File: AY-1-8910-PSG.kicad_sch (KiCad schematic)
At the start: 2 parts

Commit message: first draft
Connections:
- net GND: now reaches U?.1 (GND)
- net GND: now also A?.29 (GND), A?.4 (GND)
- net at U?.22 (CLOCK): now also A?.12 (D9)
- net A2: now reaches U?.27 (BDIR)
- net A2: now also A?.21 (A2)
- net A1: now reaches U?.28 (BC2)
- net A1: now also A?.20 (A1)
- net A0: now reaches U?.29 (BC1)
- net A0: now also A?.19 (A0)
- net A3: now reaches U?.30 (DA7)
- net A3: now also A?.22 (A3)
- net at U?.31 (DA6): now also A?.11 (D8)
- net at U?.32 (DA5): now also A?.10 (D7)
- net at U?.33 (DA4): now also A?.9 (D6)
- net at U?.34 (DA3): now also A?.8 (D5)
- net at U?.35 (DA2): now also A?.7 (D4)
- net at U?.36 (DA1): now also A?.6 (D3)
- net at U?.37 (DA0): now also A?.5 (D2)
- net +5V: now reaches U?.40 (VCC)
- net +5V: now also A?.27 (+5V)
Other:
- moved on the sheet: A?
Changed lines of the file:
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@@
 (kicad_sch (version 20211123) (generator eeschema)
   (paper "A4")
+  (wire (pts (xy 139.7 80.01) (xy 167.64 80.01))
+    (stroke (width 0) (type default) (color 0 0 0 0))
+  )
+  (wire (pts (xy 139.7 82.55) (xy 167.64 82.55))
+    (stroke (width 0) (type default) (color 0 0 0 0))
+  )
+  (wire (pts (xy 139.7 115.57) (xy 154.94 115.57))
+    (stroke (width 0) (type default) (color 0 0 0 0))
+  )
+  (wire (pts (xy 87.63 69.85) (xy 99.06 69.85))
+    (stroke (width 0) (type default) (color 0 0 0 0))
+  )
+  (wire (pts (xy 139.7 92.71) (xy 167.64 92.71))
+    (stroke (width 0) (type default) (color 0 0 0 0))
+  )
+  (wire (pts (xy 154.94 95.25) (xy 154.94 115.57))
+    (stroke (width 0) (type default) (color 0 0 0 0))
+  )
+  (wire (pts (xy 139.7 77.47) (xy 167.64 77.47))
+    (stroke (width 0) (type default) (color 0 0 0 0))
+  )
+  (wire (pts (xy 167.64 95.25) (xy 154.94 95.25))
+    (stroke (width 0) (type default) (color 0 0 0 0))
+  )
+  (wire (pts (xy 139.7 90.17) (xy 167.64 90.17))
+    (stroke (width 0) (type default) (color 0 0 0 0))
+  )
+  (wire (pts (xy 139.7 87.63) (xy 167.64 87.63))
+    (stroke (width 0) (type default) (color 0 0 0 0))
+  )
+  (wire (pts (xy 139.7 85.09) (xy 167.64 85.09))
+    (stroke (width 0) (type default) (color 0 0 0 0))
+  )
+  (global_label "A3" (shape input) (at 139.7 95.25 0) (fields_autoplaced)
+    (effects (font (size 1.27 1.27)) (justify left))
+    (property "Intersheet References" "${INTERSHEET_REFS}" (id 0) (at 144.4112 95.1706 0)
+      (effects (font (size 1.27 1.27)) (justify left) hide)
+    )
+  )
+  (global_label "A0" (shape input) (at 139.7 97.79 0) (fields_autoplaced)
+    (effects (font (size 1.27 1.27)) (justify left))
+    (property "Intersheet References" "${INTERSHEET_REFS}" (id 0) (at 144.4112 97.7106 0)
+      (effects (font (size 1.27 1.27)) (justify left) hide)
+    )
+  )
+  (global_label "A1" (shape input) (at 139.7 100.33 0) (fields_autoplaced)
+    (effects (font (size 1.27 1.27)) (justify left))
+    (property "Intersheet References" "${INTERSHEET_REFS}" (id 0) (at 144.4112 100.2506 0)
+      (effects (font (size 1.27 1.27)) (justify left) hide)
+    )
+  )
+  (global_label "A2" (shape input) (at 193.04 95.25 0) (fields_autoplaced)
+    (effects (font (size 1.27 1.27)) (justify left))
+    (property "Intersheet References" "${INTERSHEET_REFS}" (id 0) (at 197.7512 95.1706 0)
+      (effects (font (size 1.27 1.27)) (justify left) hide)
+    )
+  )
+  (global_label "A1" (shape input) (at 193.04 92.71 0) (fields_autoplaced)
+    (effects (font (size 1.27 1.27)) (justify left))
+    (property "Intersheet References" "${INTERSHEET_REFS}" (id 0) (at 197.7512 92.6306 0)
+      (effects (font (size 1.27 1.27)) (justify left) hide)
+    )
+  )
+  (global_label "A2" (shape input) (at 139.7 102.87 0) (fields_autoplaced)
+    (effects (font (size 1.27 1.27)) (justify left))
+    (property "Intersheet References" "${INTERSHEET_REFS}" (id 0) (at 144.4112 102.7906 0)
+      (effects (font (size 1.27 1.27)) (justify left) hide)
+    )
+  )
+  (global_label "A0" (shape input) (at 193.04 90.17 0) (fields_autoplaced)
+    (effects (font (size 1.27 1.27)) (justify left))
+    (property "Intersheet References" "${INTERSHEET_REFS}" (id 0) (at 197.7512 90.0906 0)
+      (effects (font (size 1.27 1.27)) (justify left) hide)
+    )
+  )
+  (global_label "A3" (shape input) (at 193.04 97.79 0) (fields_autoplaced)
+    (effects (font (size 1.27 1.27)) (justify left))
+    (property "Intersheet References" "${INTERSHEET_REFS}" (id 0) (at 197.7512 97.7106 0)
+      (effects (font (size 1.27 1.27)) (justify left) hide)
+    )
+  )
   (symbol (lib_id "xenir_v6:AY-3-8910") (at 119.38 62.23 0) (unit 1)
     (in_bom yes) (on_board yes) (fields_autoplaced)
@@
     (pin "9")
   )
-  (symbol (lib_id "MCU_Module:Arduino_Nano_Every") (at 180.34 92.71 0) (unit 1)
-    (in_bom yes) (on_board yes) (fields_autoplaced)
-    (property "Reference" "A?" (id 0) (at 182.3594 118.11 0)
+  (symbol (lib_id "power:GND") (at 87.63 69.85 0) (unit 1)
+    (in_bom yes) (on_board yes) (fields_autoplaced)
+    (property "Reference" "#PWR?" (id 0) (at 87.63 76.2 0)
+      (effects (font (size 1.27 1.27)) hide)
+    )
+    (property "Value" "GND" (id 1) (at 87.63 74.93 0))
+    (property "Footprint" "" (id 2) (at 87.63 69.85 0)
+      (effects (font (size 1.27 1.27)) hide)
+    )
+    (property "Datasheet" "" (id 3) (at 87.63 69.85 0)
+      (effects (font (size 1.27 1.27)) hide)
+    )
+    (pin "1")
+  )
+  (symbol (lib_id "power:GND") (at 180.34 115.57 0) (unit 1)
+    (in_bom yes) (on_board yes) (fields_autoplaced)
+    (property "Reference" "#PWR?" (id 0) (at 180.34 121.92 0)
+      (effects (font (size 1.27 1.27)) hide)
+    )
+    (property "Value" "GND" (id 1) (at 180.34 120.65 0))
+    (property "Footprint" "" (id 2) (at 180.34 115.57 0)
+      (effects (font (size 1.27 1.27)) hide)
+    )
+    (property "Datasheet" "" (id 3) (at 180.34 115.57 0)
+      (effects (font (size 1.27 1.27)) hide)
+    )
+    (pin "1")
+  )
+  (symbol (lib_id "power:+5V") (at 139.7 69.85 0) (unit 1)
+    (in_bom yes) (on_board yes) (fields_autoplaced)
+    (property "Reference" "#PWR?" (id 0) (at 139.7 73.66 0)
+      (effects (font (size 1.27 1.27)) hide)
+    )
+    (property "Value" "+5V" (id 1) (at 139.7 64.77 0))
+    (property "Footprint" "" (id 2) (at 139.7 69.85 0)
+      (effects (font (size 1.27 1.27)) hide)
+    )
+    (property "Datasheet" "" (id 3) (at 139.7 69.85 0)
+      (effects (font (size 1.27 1.27)) hide)
+    )
+    (pin "1")
+  )
+  (symbol (lib_id "power:+5V") (at 185.42 64.77 0) (unit 1)
+    (in_bom yes) (on_board yes) (fields_autoplaced)
+    (property "Reference" "#PWR?" (id 0) (at 185.42 68.58 0)
+      (effects (font (size 1.27 1.27)) hide)
+    )
+    (property "Value" "+5V" (id 1) (at 185.42 59.69 0))
+    (property "Footprint" "" (id 2) (at 185.42 64.77 0)
+      (effects (font (size 1.27 1.27)) hide)
+    )
+    (property "Datasheet" "" (id 3) (at 185.42 64.77 0)
+      (effects (font (size 1.27 1.27)) hide)
+    )
+    (pin "1")
+  )
+  (symbol (lib_id "MCU_Module:Arduino_Nano_Every") (at 180.34 90.17 0) (unit 1)
+    (in_bom yes) (on_board yes) (fields_autoplaced)
+    (property "Reference" "A?" (id 0) (at 182.3594 115.57 0)
       (effects (font (size 1.27 1.27)) (justify left))
     )
-    (property "Value" "Arduino_Nano_Every" (id 1) (at 182.3594 120.65 0)
+    (property "Value" "Arduino_Nano_Every" (id 1) (at 182.3594 118.11 0)
       (effects (font (size 1.27 1.27)) (justify left))
     )
-    (property "Footprint" "Module:Arduino_Nano" (id 2) (at 180.34 92.71 0)
+    (property "Footprint" "Module:Arduino_Nano" (id 2) (at 180.34 90.17 0)
       (effects (font (size 1.27 1.27) italic) hide)
     )
-    (property "Datasheet" "https://content.arduino.cc/assets/NANOEveryV3.0_sch.pdf" (id 3) (at 180.34 92.71 0)
+    (property "Datasheet" "https://content.arduino.cc/assets/NANOEveryV3.0_sch.pdf" (id 3) (at 180.34 90.17 0)
       (effects (font (size 1.27 1.27)) hide)
     )
@@
   )
   (symbol_instances
+    (path "/318a80bc-bb47-479b-9ad6-cc89ccf1f537"
+      (reference "#PWR?") (unit 1) (value "GND") (footprint "")
+    )
+    (path "/79c82aa0-68c2-4c99-9665-4d614e59696c"
+      (reference "#PWR?") (unit 1) (value "GND") (footprint "")
+    )
+    (path "/a2348e69-57ed-4427-8ba5-b20356f146a3"
+      (reference "#PWR?") (unit 1) (value "+5V") (footprint "")
+    )
+    (path "/d8b2571c-5c58-4db9-bc3d-b5cf98bfa251"
+      (reference "#PWR?") (unit 1) (value "+5V") (footprint "")
+    )
     (path "/e9678172-8957-4dd3-80d7-8fc9e74cf769"
       (reference "A?") (unit 1) (value "Arduino_Nano_Every") (footprint "Module:Arduino_Nano")

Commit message: update
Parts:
- added C1: 220uF, symbol Device:C_Polarized
- added C2: 47nF, symbol xenir:Capacitor
- added C3: 220nF, symbol xenir:Capacitor
- added C?: 10uF, symbol Device:C_Polarized
- added R1: 10, symbol xenir:Resistor
- added R2: 510, symbol xenir:Resistor
- added R3: 5.1k, symbol xenir:Resistor
- added R4: 1k, symbol xenir:Resistor
- added U1: LM386, symbol Amplifier_Audio:LM386
- gave numbers to parts that had none: 2
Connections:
- net GND: now also C3.1, C?.2, R1.1, R2.1, R4.1, U1.2 (-), U1.4 (GND)
- net at U2.3 (CHAN_B): now also U2.38 (CHAN_C), U2.4 (CHAN_A), R3.1, R4.2
- new net: C3.2, R2.2, R3.2, U1.3 (+)
- new net: C2.1, R1.2
- new net: C1.1, C2.2, U1.5
- new net +10V: C?.1, U1.6 (V+)
- new net AUDIO_OUT: C1.2
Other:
- moved on the sheet: A1, U2

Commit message: gg
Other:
- note added: "Bus Control"
- note added: "Data Lines"
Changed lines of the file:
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@@
     (stroke (width 0) (type default) (color 0 0 0 0))
+  )
+  (text "Bus\nControl" (at 195.58 109.22 90)
+    (effects (font (size 1.27 1.27)) (justify left bottom))
+  )
+  (text "Data Lines" (at 203.2 96.52 90)
+    (effects (font (size 1.27 1.27)) (justify left bottom))
   )
   (global_label "A3" (shape input) (at 186.69 100.33 0) (fields_autoplaced)

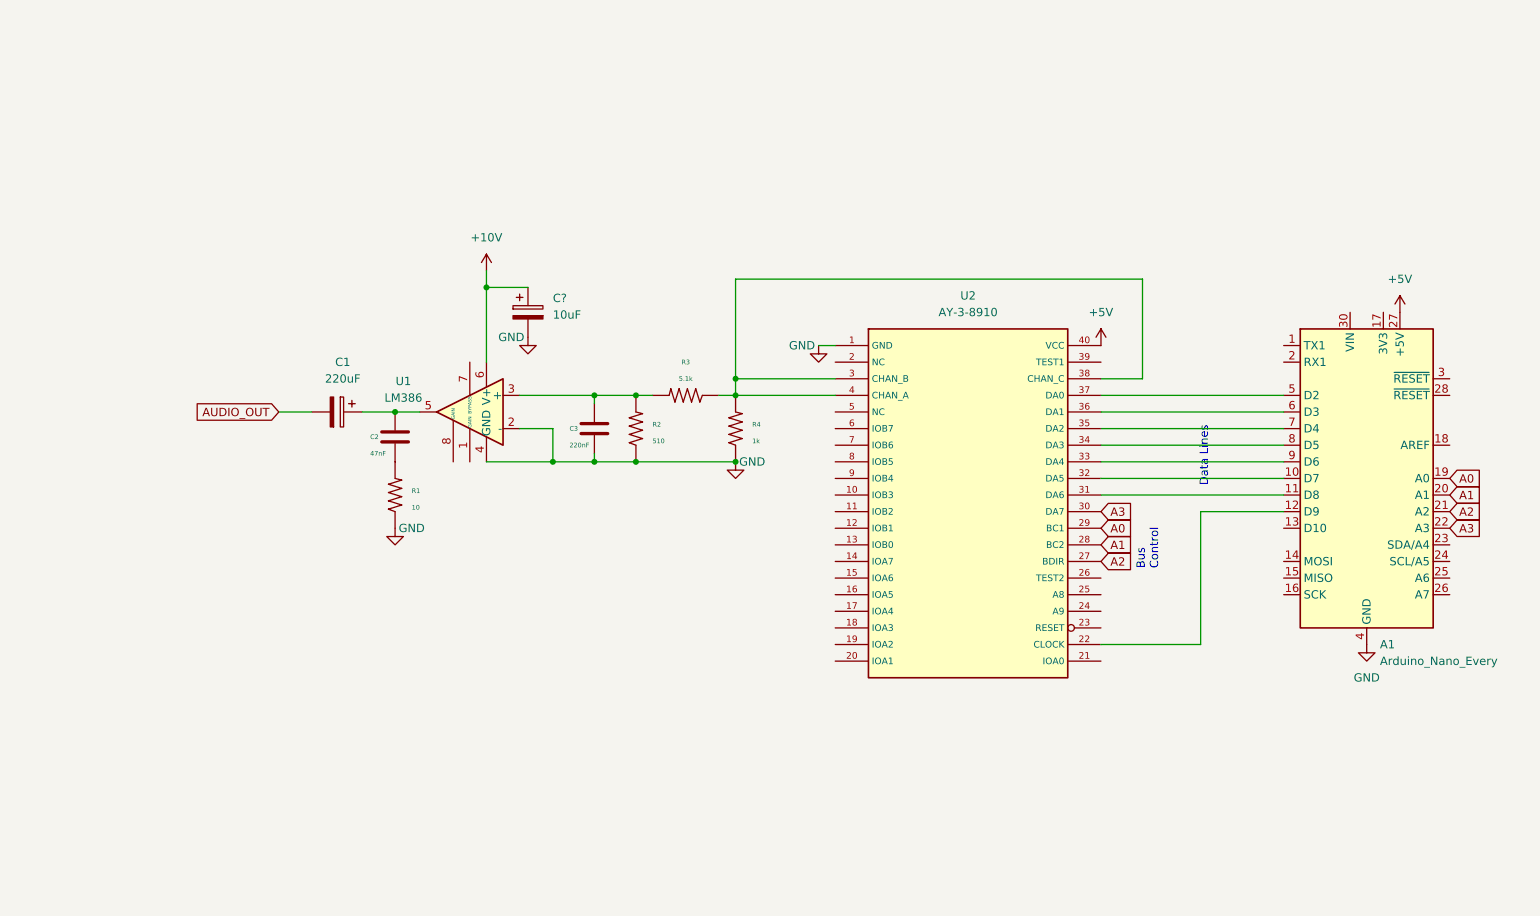
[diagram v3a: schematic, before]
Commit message: added esp32
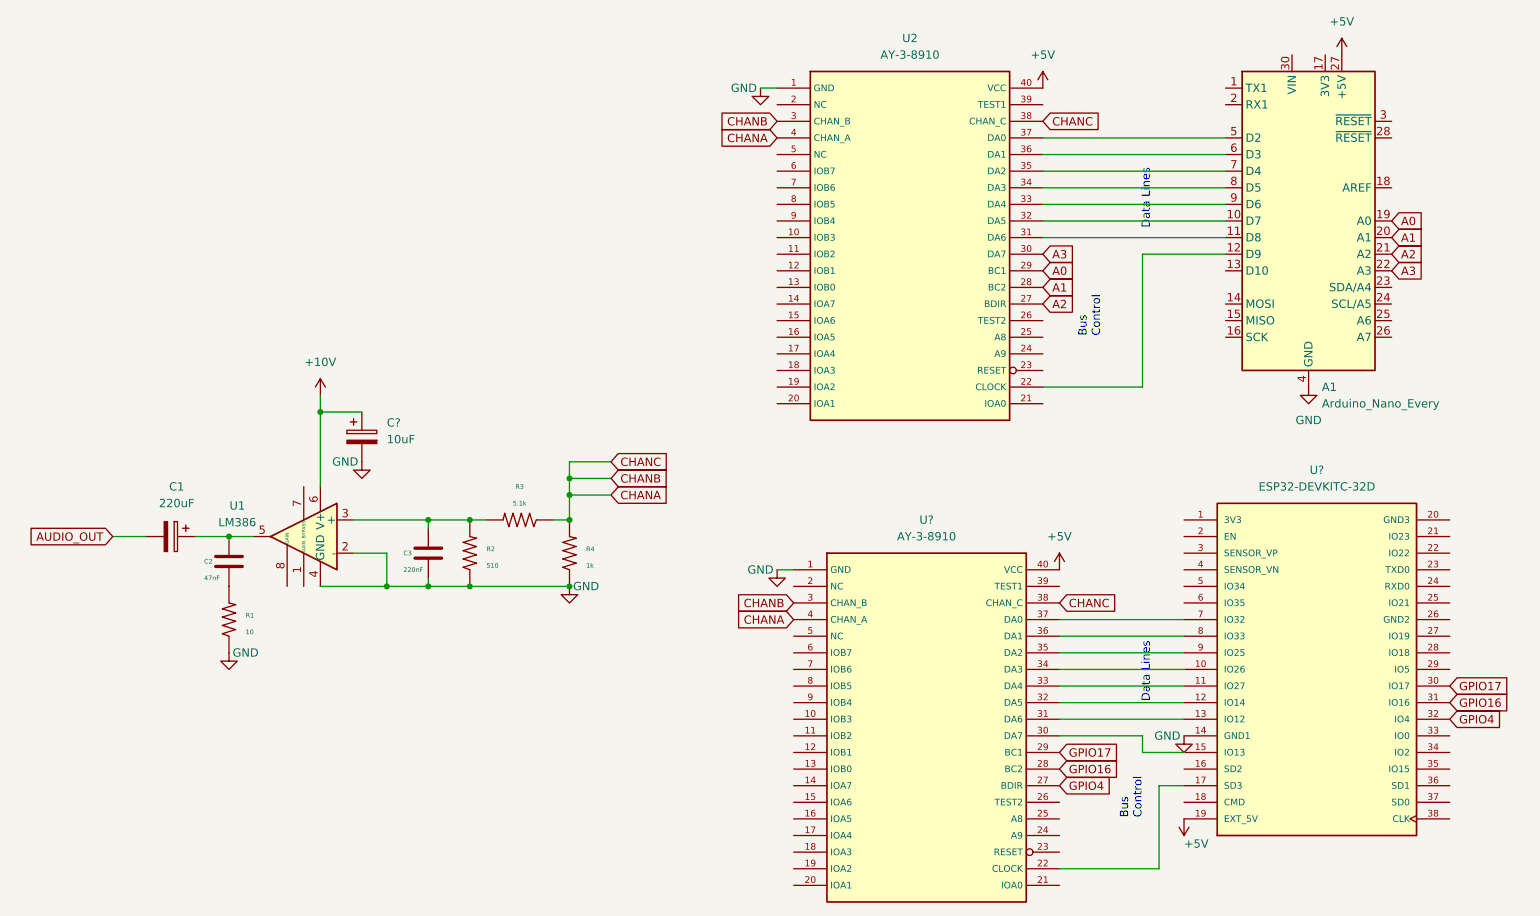
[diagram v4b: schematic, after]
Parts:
- added U?: ESP32-DEVKITC-32D, symbol xenir:ESP32-DEVKITC-32D
- added U?: AY-3-8910, symbol xenir_v6:AY-3-8910
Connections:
- net +5V: now also U?.19 (EXT_5V), U?.40 (VCC)
- net GND: now also U?.1 (GND), U?.14 (GND1)
- net CHANA: now reaches R3.1, R4.2, U2.3 (CHAN_B), U2.38 (CHAN_C), U2.4 (CHAN_A)
- net CHANA: now also U?.3 (CHAN_B), U?.38 (CHAN_C), U?.4 (CHAN_A)
- new net: U?.10 (IO26), U?.34 (DA3)
- new net: U?.11 (IO27), U?.33 (DA4)
- new net: U?.12 (IO14), U?.32 (DA5)
- new net: U?.13 (IO12), U?.31 (DA6)
- new net: U?.15 (IO13), U?.30 (DA7)
- new net: U?.17 (SD3), U?.22 (CLOCK)
- new net: U?.37 (DA0), U?.7 (IO32)
- new net: U?.36 (DA1), U?.8 (IO33)
- new net: U?.35 (DA2), U?.9 (IO25)
- new net GPIO16: U?.28 (BC2), U?.31 (IO16)
- new net GPIO17: U?.29 (BC1), U?.30 (IO17)
- new net GPIO4: U?.27 (BDIR), U?.32 (IO4)
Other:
- moved on the sheet: A1, C1, C2, C3, C?, R1, R2, R3, R4, U1, U2
